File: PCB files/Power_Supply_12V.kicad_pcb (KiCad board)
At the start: 2 copper layers, 75.3 x 28 mm, 16 parts, among them J1 Input, J2 Output, U1 LM7812_TO220, U2 LM7912_TO220

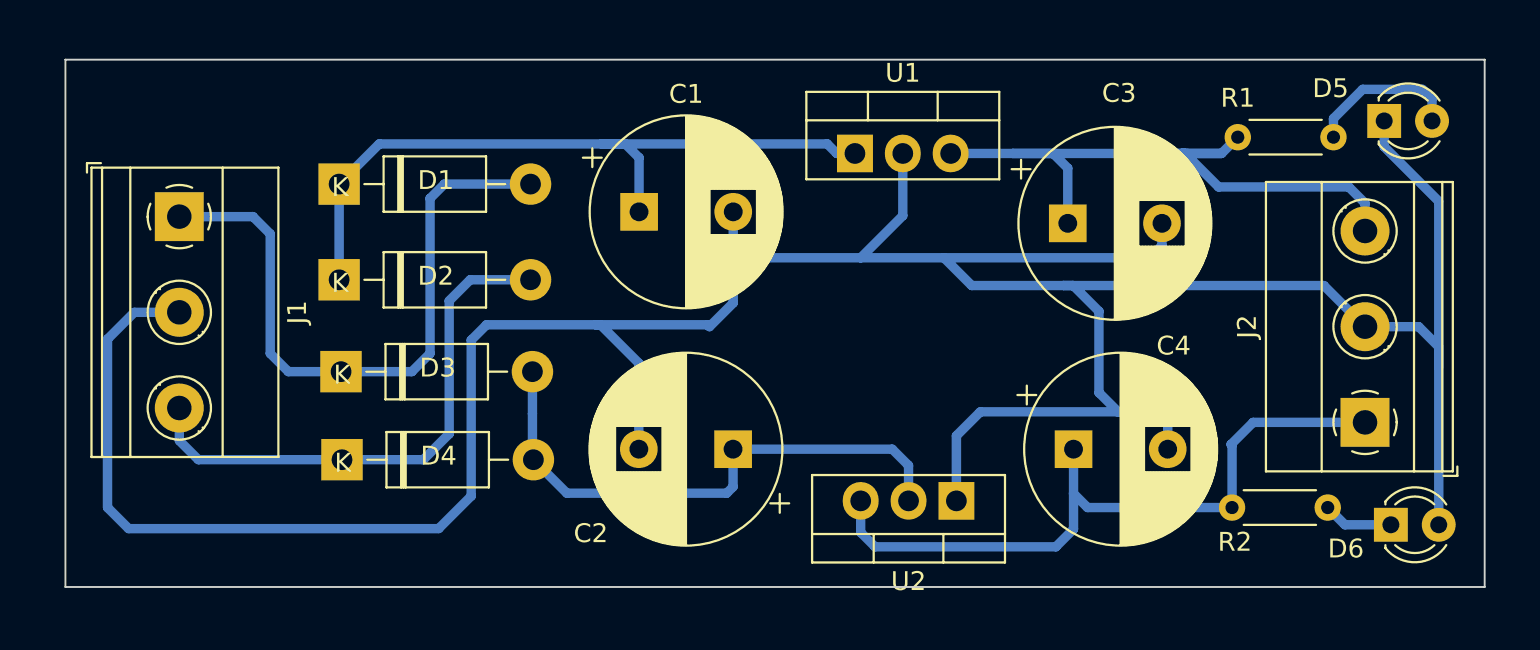
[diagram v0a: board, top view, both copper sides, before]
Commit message: Changed track width
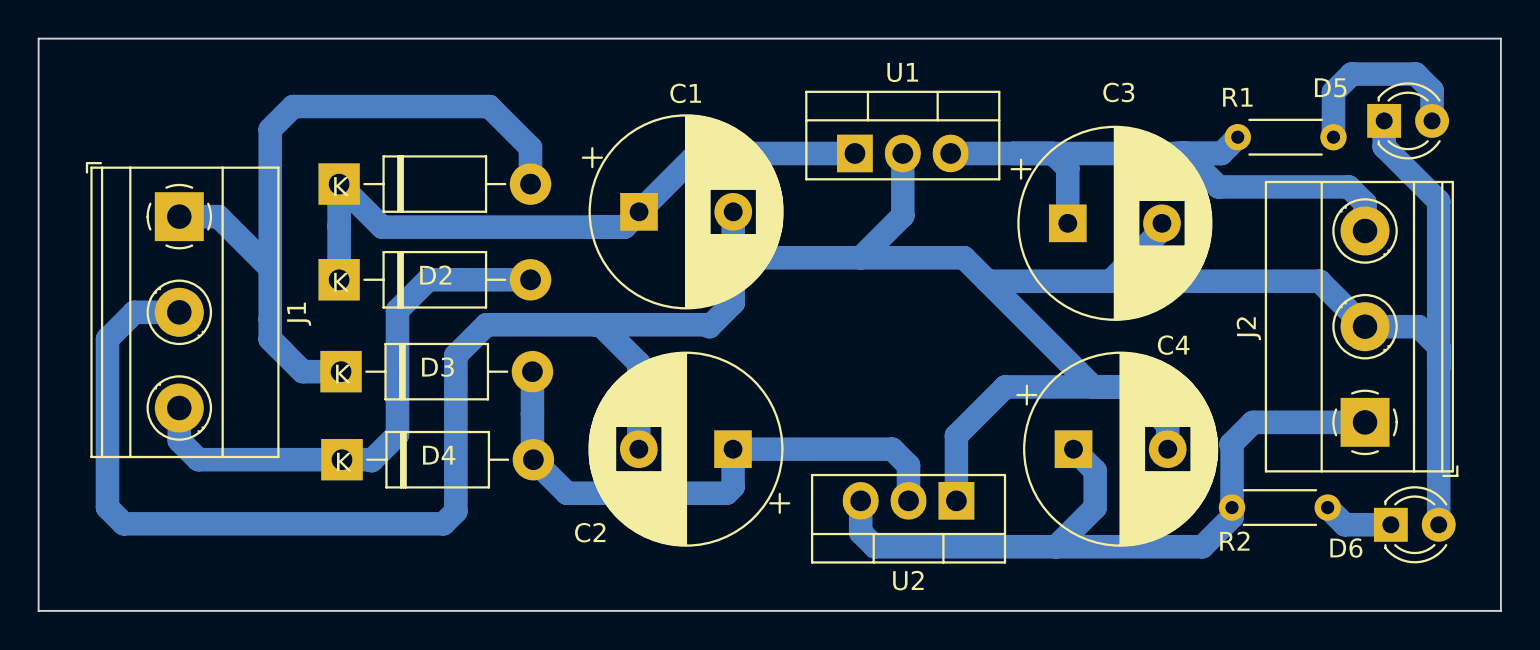
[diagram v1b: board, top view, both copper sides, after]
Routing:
- net Net-(D1-A): track 34.7 -> 46.4 mm
- net Net-(D5-K): track 177.2 -> 170.9 mm
- net Net-(J2-Pin_1): track 37.6 -> 40.4 mm
- net Net-(D5-A): track 8.24 -> 10.0 mm
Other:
- board size 75.3 x 28 mm -> 77.6 x 30.4 mm
